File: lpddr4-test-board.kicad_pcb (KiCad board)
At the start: 8 copper layers, 117 x 86 mm, 240 parts, among them IC1 TPS54561, IC3 TPD8S009DSMR, J1 0878311420, J10 61300311121, J2 08B0-1X1T-36-F, J3 DC_SOCKET, J4 WE_629105150521, J5 2309409-1, J6 685119134923, J7 1140084168, Q2 BSS138APW, Q3 BSS138APW, Q4 BSS138APW, Q5 BSS138APW, Q6 BSS138APW, Q7 BSS138APW, Q8 BSS138APW, U1 XC7K70T-FBG484, U2 ASEM1-100.000MHZ-LC-T, U3 S25FL128SAGNFI000, U4 TPS65296, U5 TPS62823DLCT, U6 DP83848JSQ_NOPB, U7 FT4232HQ, Y1 ABM8G-25.000MHZ-18-D2Y-T

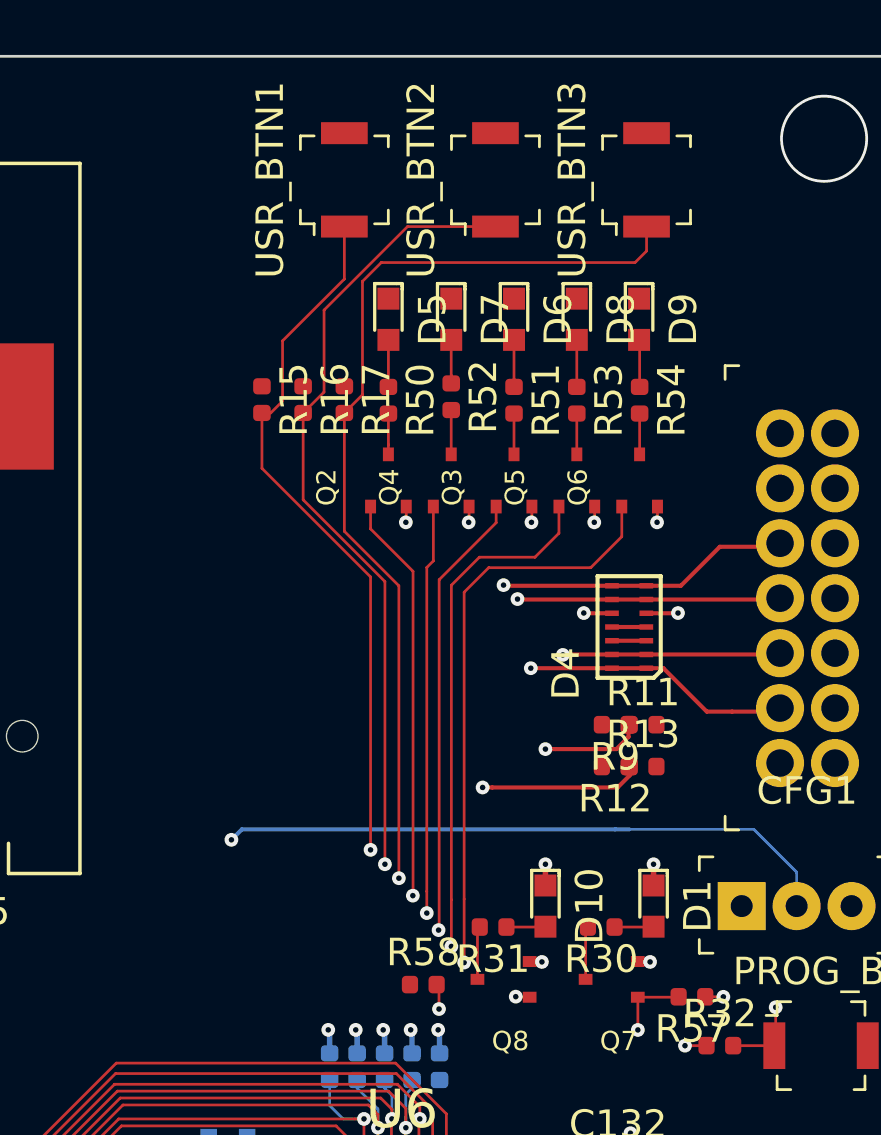
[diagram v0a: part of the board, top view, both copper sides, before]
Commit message: Move buttons under LEDs
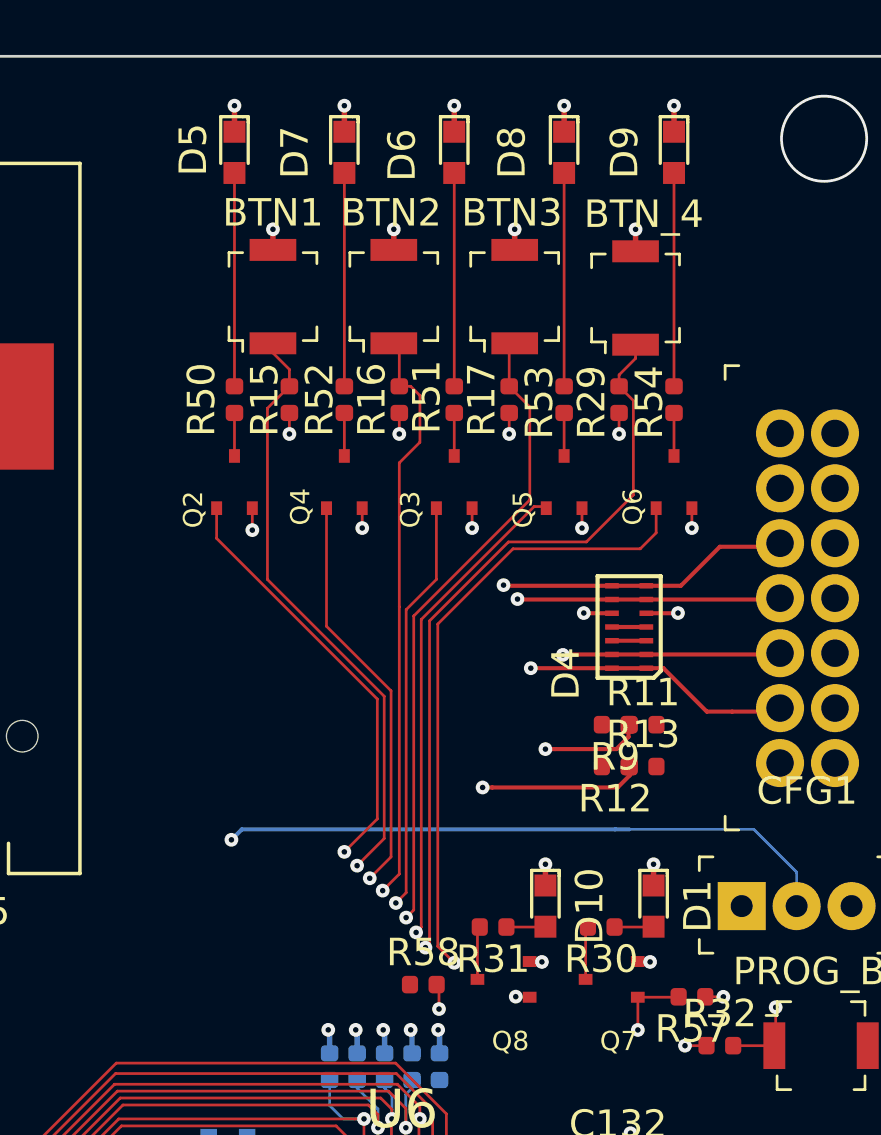
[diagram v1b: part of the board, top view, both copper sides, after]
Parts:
- removed USR_BTN1, USR_BTN2: B3U-1000P, lpddr4-test-board-footprints:Switch_Tactile_SMD_B3U-1000P
- added BTN1: B3U-1000P, lpddr4-test-board-footprints:Switch_Tactile_SMD_B3U-1000P, F.Cu at (193.9, 58.7)
- added BTN2: B3U-1000P, lpddr4-test-board-footprints:Switch_Tactile_SMD_B3U-1000P, F.Cu at (198.3, 58.7)
- added BTN_4: B3U-1000P, lpddr4-test-board-footprints:Switch_Tactile_SMD_B3U-1000P, F.Cu at (207.1, 58.8)
- added R29: R_4k7_0402, lpddr4-test-board-footprints:0402-res, F.Cu at (206.5, 62.5)
- moved D5 8.26 mm to (192.5, 53.5)
- moved D7 7.21 mm to (196.5, 53.5)
- moved D6 6.45 mm to (200.5, 53.5)
- moved BTN3 6.41 mm to (202.7, 58.7)
- moved D9 6.21 mm to (208.5, 53.5)
- moved D8 6.09 mm to (204.5, 53.5)
- moved R17 6.00 mm to (202.5, 62.5), turned to 90 degrees
- moved Q2 5.60 mm to (192.5, 65.5)
- moved R50 5.60 mm to (192.5, 62.5)
- moved R52 3.89 mm to (196.5, 62.5)
- moved Q4 3.89 mm to (196.5, 65.5)
- moved R16 3.50 mm to (198.5, 62.5), turned to 90 degrees
- moved Q3 2.18 mm to (200.5, 65.5)
- moved R51 2.18 mm to (200.5, 62.5)
- moved Q6 1.25 mm to (208.5, 65.5)
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- renumbered USR_BTN3 to BTN3
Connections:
- U1 pad A8: USR_LED2 -> USR_LED3
- U1 pad B8: USR_LED1 -> USR_BTN2
- U1 pad C8: USR_BTN3 -> USR_LED2
- U1 pad C9: USR_LED3 -> USR_BTN3
- U1 pad E8: USR_BTN2 -> USR_BTN1
- U1 pad E9: USR_LED5 -> USR_BTN4
- U1 pad F8: USR_BTN1 -> USR_LED1
- U1 pad F9: Net-(U1-PadF9) -> USR_LED5
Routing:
- net USR_BTN4: track 0.00 -> 56.4 mm, vias 0 -> 2
- net USR_BTN2: track 57.1 -> 45.5 mm
- net USR_BTN3: track 60.7 -> 49.6 mm
- net Net-(D7-Pad2): track 1.58 -> 7.77 mm
- net Net-(D8-Pad2): track 1.71 -> 7.77 mm
- net Net-(D6-Pad2): track 1.71 -> 7.77 mm
- net Net-(D5-Pad2): track 1.71 -> 7.77 mm
- net Net-(D9-Pad2): track 1.72 -> 7.77 mm
- net USR_BTN1: track 54.3 -> 48.6 mm
- net USR_LED3: track 43.7 -> 38.7 mm
- net VCC3V3: track 69.7 -> 74.5 mm, vias 36 -> 41
- net GND: track 169.5 -> 173.5 mm, vias 180 -> 184
- net VCC3v3: track 5.09 -> 8.15 mm, vias 7 -> 11
- net USR_LED1: track 40.2 -> 43.0 mm
- net USR_LED5: track 51.5 -> 54.1 mm
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
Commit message: Add power planes - WIP
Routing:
- net VCC5V0: vias 15 -> 25
- added copper zone on F.Cu, net Net-(C178-Pad1)
- added copper zone on F.Cu, net Net-(C35-Pad1)
- added copper zone on B.Cu, net Net-(C45-Pad1)
- added copper zone on VCC2, net VDDQ
- removed copper zone on F.Cu, net (none)
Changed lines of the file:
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@@
     (thickness 1.6)
     (drawings 130)
-    (tracks 2935)
+    (tracks 2944)
     (zones 0)
     (modules 242)
@@
   (segment (start 102.564 120.784485) (end 102.564 120.03) (width 0.25) (layer F.Cu) (net 334))
   (segment (start 102.536328 120.812157) (end 102.564 120.784485) (width 0.25) (layer F.Cu) (net 334))
-  (segment (start 132.954 91.47) (end 132.954 91.74) (width 0.25) (layer F.Cu) (net 338))
   (segment (start 117.464 84.35) (end 125.834 84.35) (width 0.25) (layer F.Cu) (net 338))
   (segment (start 123.004 112.03) (end 123.756463 112.03) (width 0.25) (layer F.Cu) (net 338))
@@
   (segment (start 208.536328 64.547157) (end 208.536328 62.982157) (width 0.1) (layer F.Cu) (net 111))
   (segment (start 208.536328 62.012157) (end 208.536328 54.247157) (width 0.1) (layer F.Cu) (net 114))
+  (via (at 127.536328 111.247157) (size 0.5) (drill 0.2) (layers F.Cu B.Cu) (net 334))
+  (via (at 128.536328 111.247157) (size 0.5) (drill 0.2) (layers F.Cu B.Cu) (net 334))
+  (via (at 129.536328 111.247157) (size 0.5) (drill 0.2) (layers F.Cu B.Cu) (net 334))
+  (via (at 130.536328 111.247157) (size 0.5) (drill 0.2) (layers F.Cu B.Cu) (net 334))
+  (via (at 131.536328 111.247157) (size 0.5) (drill 0.2) (layers F.Cu B.Cu) (net 334))
+  (via (at 127.536328 112.247157) (size 0.5) (drill 0.2) (layers F.Cu B.Cu) (net 334))
+  (via (at 128.536328 112.247157) (size 0.5) (drill 0.2) (layers F.Cu B.Cu) (net 334))
+  (via (at 129.536328 112.247157) (size 0.5) (drill 0.2) (layers F.Cu B.Cu) (net 334))
+  (via (at 130.536328 112.247157) (size 0.5) (drill 0.2) (layers F.Cu B.Cu) (net 334))
+  (via (at 131.536328 112.247157) (size 0.5) (drill 0.2) (layers F.Cu B.Cu) (net 334))
   (segment (start 176.896318 91.137168) (end 184.301341 91.137168) (width 0.1) (layer In2.Cu) (net 639))
   (segment (start 176.036329 91.997157) (end 176.896318 91.137168) (width 0.1) (layer In2.Cu) (net 639))
@@
     (polygon
       (pts
-        (xy 111.534 135.82) (xy 107.874 135.82) (xy 107.874 121.71) (xy 106.324 121.71) (xy 106.324 118.21)
-        (xy 108.904 118.22) (xy 108.904 120.45) (xy 111.534 120.45)
+        (xy 133.536328 135.82) (xy 107.874 135.82) (xy 107.874 121.71) (xy 106.324 121.71) (xy 106.324 118.21)
+        (xy 108.904 118.22) (xy 108.904 120.45) (xy 133.536328 120.45)
       )
     )
@@
     (polygon
       (pts
-        (xy 125.786328 101.54) (xy 122.454 109.94) (xy 122.454 110.84) (xy 122.054 110.84) (xy 122.054 109.54)
+        (xy 125.786328 106.597157) (xy 122.454 109.94) (xy 122.454 110.84) (xy 122.054 110.84) (xy 122.054 109.54)
         (xy 122.354 109.24) (xy 122.354 90.14) (xy 125.786328 90.14)
       )
@@
     (polygon
       (pts
-        (xy 110.694 88.23) (xy 100.024 88.23) (xy 100.024 85.73) (xy 110.694 85.73)
+        (xy 110.694 88.23) (xy 102.536328 88.23) (xy 102.536328 85.73) (xy 110.694 85.73)
       )
     )
@@
     (polygon
       (pts
-        (xy 129.160252 112.94) (xy 126.654 112.94) (xy 125.154 111.44) (xy 125.154 110.64) (xy 129.147748 110.64)
+        (xy 132.536328 112.94) (xy 126.654 112.94) (xy 125.154 111.44) (xy 125.154 110.64) (xy 132.536328 110.64)
       )
     )
@@
     (polygon
       (pts
-        (xy 111.164 116.26) (xy 104.404 116.26) (xy 104.404 135.98) (xy 100.004 135.98) (xy 100.004 83.6)
-        (xy 111.164 83.6)
+        (xy 111.172041 108.697157) (xy 132.536328 108.747157) (xy 132.536328 116.247157) (xy 104.404 116.26) (xy 104.404 135.98)
+        (xy 100.004 135.98) (xy 100.036328 49.997157) (xy 111.036328 49.997157)
       )
     )
@@
     )
   )
-  (zone (net 0) (net_name "") (layer F.Cu) (hatch edge 0.508)
+  (zone (net 335) (net_name "Net-(C35-Pad1)") (layer F.Cu) (hatch edge 0.508)
     (connect_pads thru_hole_only (clearance 0.2))
     (min_thickness 0.1)
@@
   )
   (zone (net 19) (net_name GND) (layer F.Cu) (hatch edge 0.508)
-    (connect_pads thru_hole_only (clearance 0.2))
+    (connect_pads yes (clearance 0.2))
     (min_thickness 0.1)
     (fill yes (arc_segments 32) (thermal_gap 0.5) (thermal_bridge_width 0.5))
@@
     )
   )
-  (zone (net 0) (net_name "") (layer F.Cu) (hatch edge 0.508)
+  (zone (net 345) (net_name "Net-(C178-Pad1)") (layer F.Cu) (hatch edge 0.508)
     (connect_pads thru_hole_only (clearance 0.2))
     (min_thickness 0.1)
@@
       )
     )
+  )
+  (zone (net 341) (net_name "Net-(C45-Pad1)") (layer B.Cu) (hatch edge 0.508)
+    (connect_pads yes (clearance 0.2))
+    (min_thickness 0.1)
+    (fill yes (arc_segments 32) (thermal_gap 0.5) (thermal_bridge_width 0.5))
+    (polygon
+      (pts
+        (xy 110.324 120.35) (xy 109.014 120.35) (xy 109.014 118.16) (xy 106.594 118.16) (xy 106.594 117.14)
+        (xy 110.324 117.14)
+      )
+    )
+  )
+  (zone (net 84) (net_name VCC3V3) (layer VCC2) (hatch edge 0.508)
+    (connect_pads yes (clearance 0.2))
+    (min_thickness 0.1)
+    (fill yes (arc_segments 32) (thermal_gap 0.5) (thermal_bridge_width 0.5))
+    (polygon
+      (pts
+        (xy 211.786328 88.997157) (xy 199.786328 100.997157) (xy 187.536328 100.997157) (xy 183.786328 104.747157) (xy 183.786328 135.997157)
+        (xy 133.036328 135.997157) (xy 133.036328 91.497157) (xy 154.036328 91.497157) (xy 154.036328 98.247157) (xy 173.536328 98.497157)
+        (xy 173.536328 91.497157) (xy 182.536328 91.497157) (xy 199.036328 74.997157)
+      )
+    )
+  )
+  (zone (net 113) (net_name VDDQ) (layer VCC2) (hatch edge 0.508)
+    (connect_pads yes (clearance 0.2))
+    (min_thickness 0.1)
+    (fill yes (arc_segments 32) (thermal_gap 0.5) (thermal_bridge_width 0.5))
+    (polygon
+      (pts
+        (xy 173.286328 98.247157) (xy 154.286328 97.997157) (xy 154.286328 89.997157) (xy 117.786328 89.997157) (xy 117.786328 83.497157)
+        (xy 173.286328 83.497157)
+      )
+    )

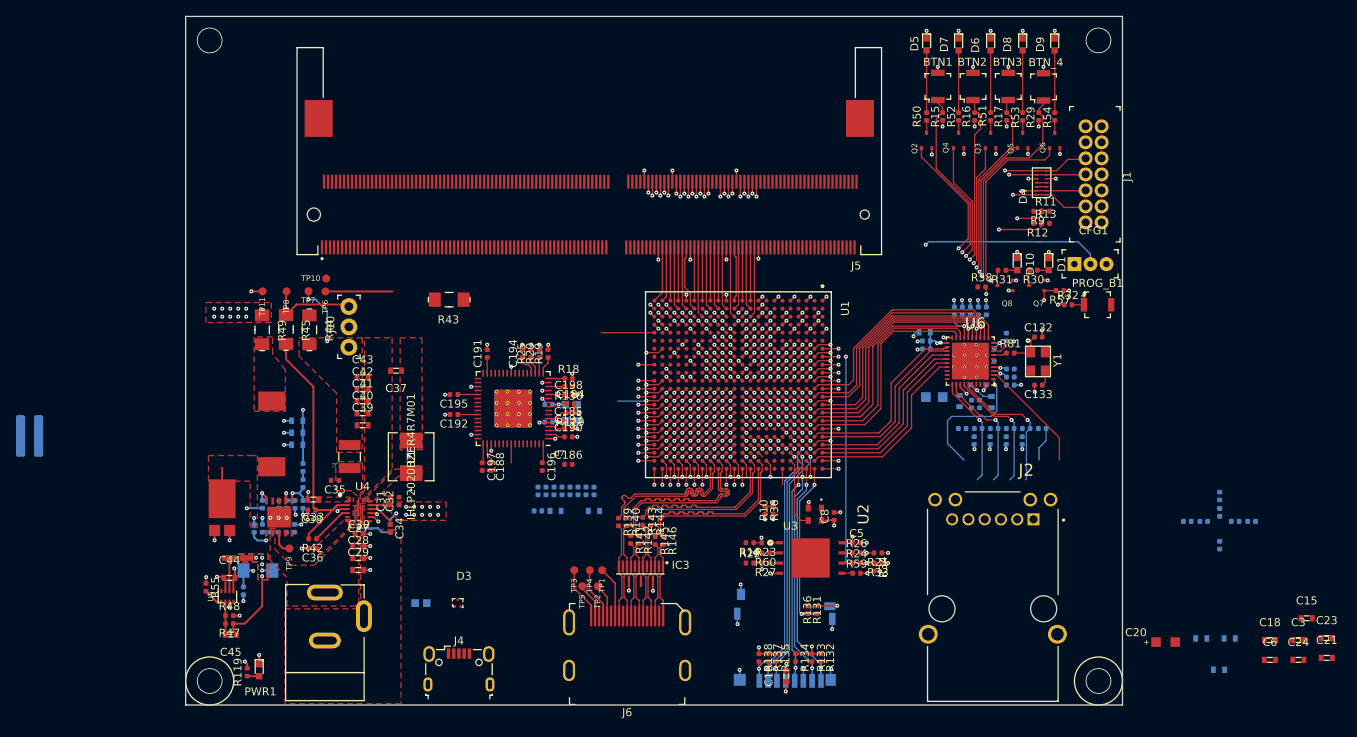
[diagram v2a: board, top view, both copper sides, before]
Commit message: Place and route new 5R1 resistor
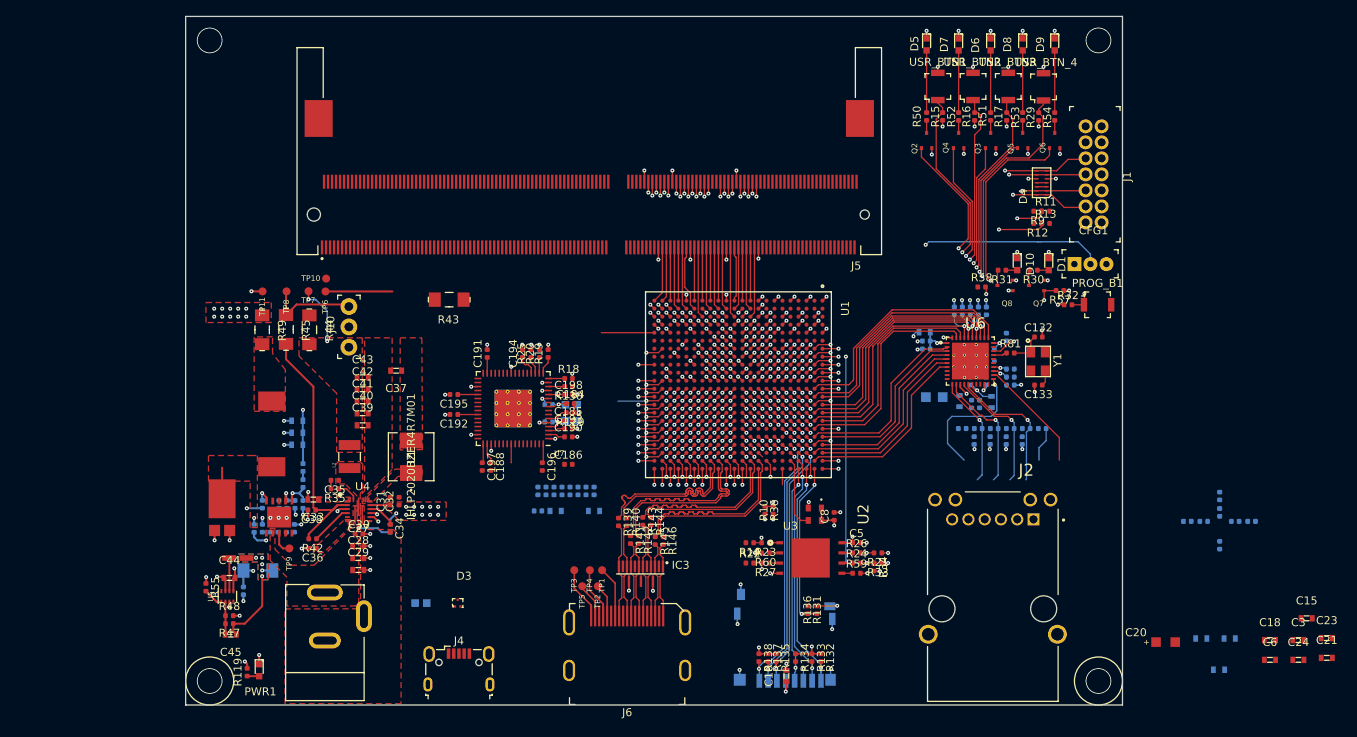
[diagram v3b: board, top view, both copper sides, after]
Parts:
- removed R41: R_5R1_1020, lpddr4-test-board-footprints:1020-res
- added R35: R_5R1_0402, antmicro-footprints:0402-res, F.Cu at (118.6, 109.0)
- renumbered BTN1 to USR_BTN1, BTN2 to USR_BTN2, BTN3 to USR_BTN3, BTN_4 to USR_BTN_4
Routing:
- net Net-(R35-Pad1): track 0.00 -> 2.69 mm
- net Net-(C35-Pad2): track 0.00 -> 1.06 mm
